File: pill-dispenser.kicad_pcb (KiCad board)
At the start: 2 copper layers, 50 x 50 mm, 34 parts, among them J1 USB-C, J2 Battery, J3 WS2812B, J4 Button, J5 Wakeup Button, Q1 AO3401A, Q2 FS8205A, U1 MT3608, U2 ESP32-C3-Zero, U3 TP4056-42-ESOP8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

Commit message: Working on 1.2 final version
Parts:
- removed J2: Battery, Connector_PinSocket_2.54mm:PinSocket_1x02_P2.54mm_Horizontal
- added BT1: Battery_Cell, Connector_PinHeader_2.54mm:PinHeader_1x02_P2.54mm_Vertical, F.Cu at (151.8, 119.7)
- added SW1: Battery Switch, EG1271:SW_EG1271, F.Cu at (150.5, 126.2)
- R11: value 1k -> 75K
- R8: value 300 -> 30K
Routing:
- net Net-(BT1--): track 0.00 -> 20.9 mm, vias 0 -> 2
- net Net-(U4-GND): track 20.5 -> 0.00 mm, vias 2 -> 0
- net VBAT: track 76.9 -> 70.6 mm, vias 2 -> 3
- net Net-(U4-VCC): track 14.6 -> 13.8 mm
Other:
- board text added: "I-Pat, LLC REV: 1.2"
- board text removed: "Telepat, LLC REV: 1.1"

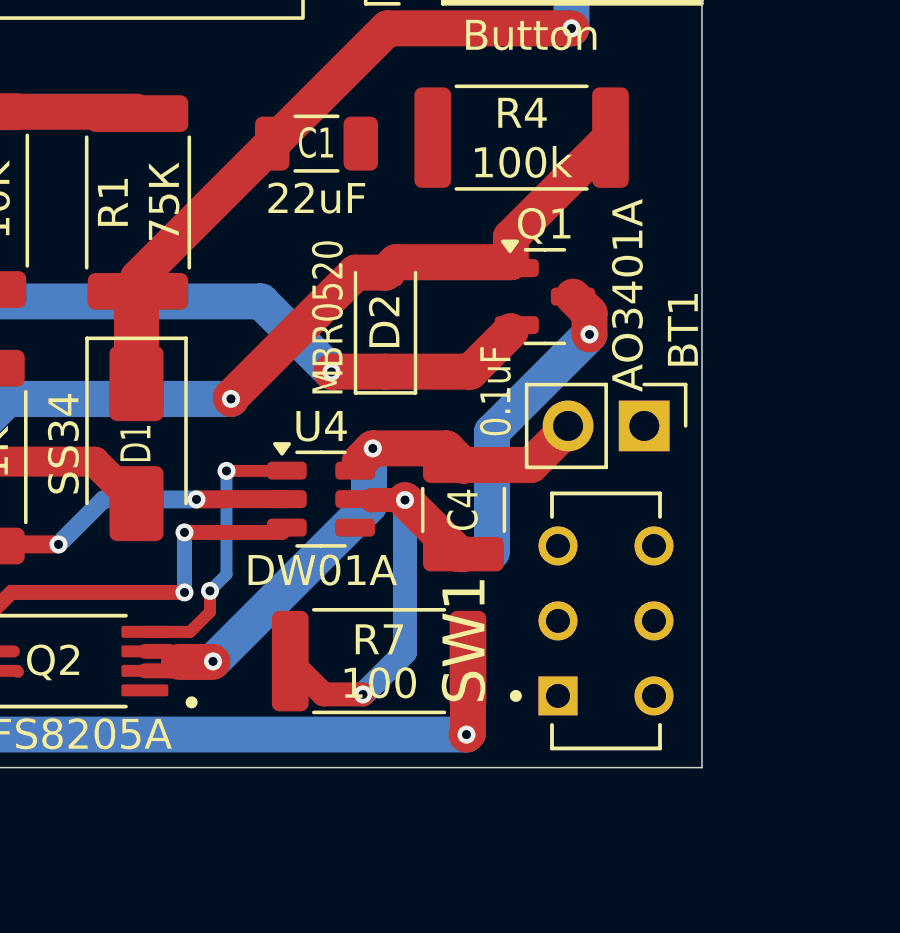
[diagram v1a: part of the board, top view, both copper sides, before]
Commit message: Updated pcb to rev1.2
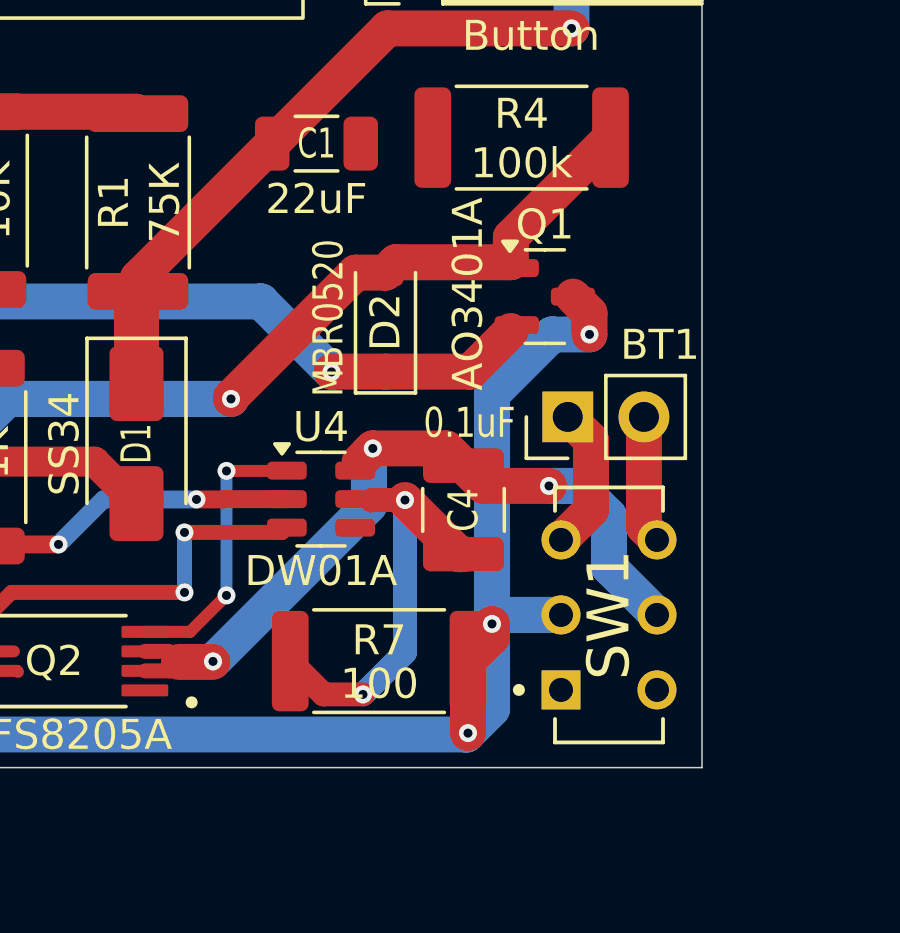
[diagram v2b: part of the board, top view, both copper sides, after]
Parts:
- moved BT1 2.57 mm to (149.2, 119.4), turned to 90 degrees
- moved SW1 0.22 mm to (150.6, 126.0)
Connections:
- SW1 pad 1: VBAT -> unconnected-(SW1-Pad1)
- SW1 pad 2: Net-(BT1-+) -> VBAT
- SW1 pad 3: unconnected-(SW1-Pad3) -> Net-(BT1-+)
- SW1 pad 4: Net-(U4-GND) -> unconnected-(SW1-Pad4)
- SW1 pad 5: Net-(BT1--) -> Net-(U4-GND)
- SW1 pad 6: unconnected-(SW1-Pad6) -> Net-(BT1--)
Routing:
- net Net-(U4-GND): track 0.00 -> 26.4 mm, vias 0 -> 3
- net Net-(BT1--): track 20.9 -> 4.28 mm, vias 2 -> 0
- net VBAT: track 70.6 -> 81.7 mm, vias 3 -> 4
- net Net-(BT1-+): track 0.00 -> 4.84 mm

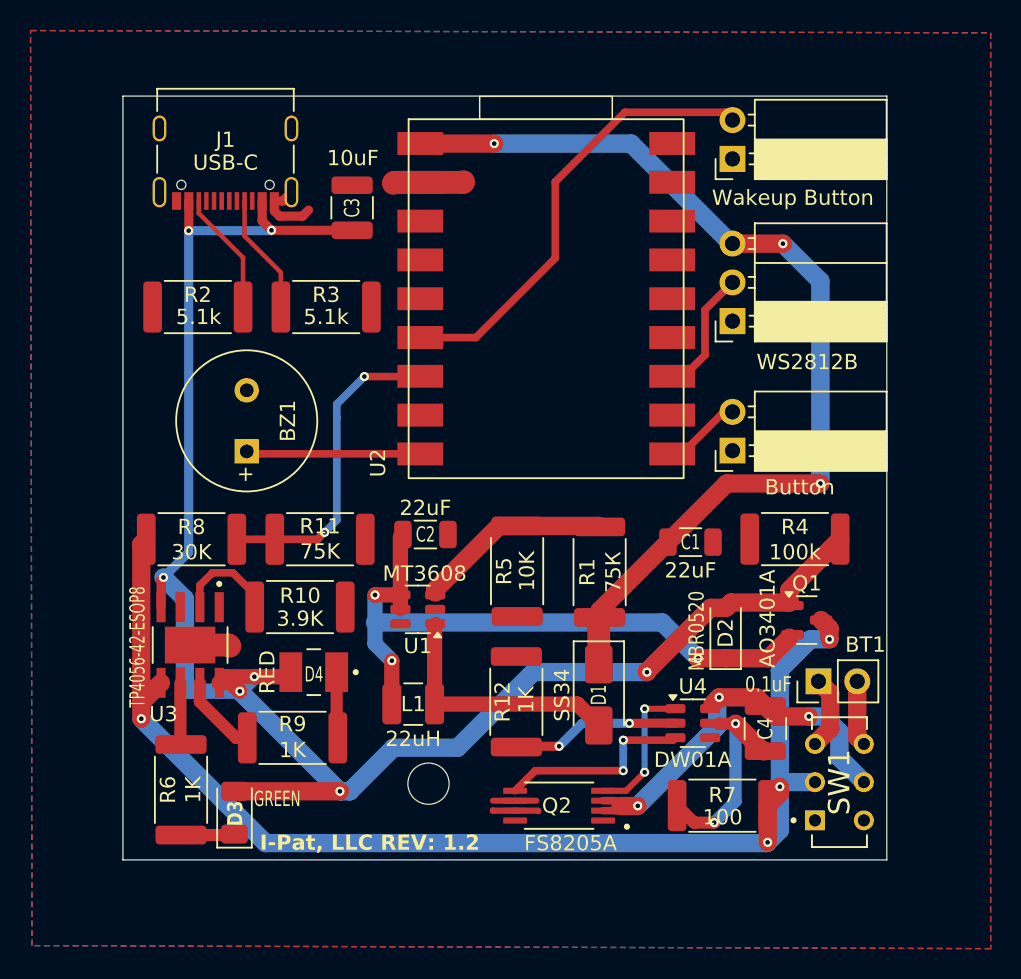
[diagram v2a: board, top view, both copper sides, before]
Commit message: Added control led strip transotor, placed buttons on PCB
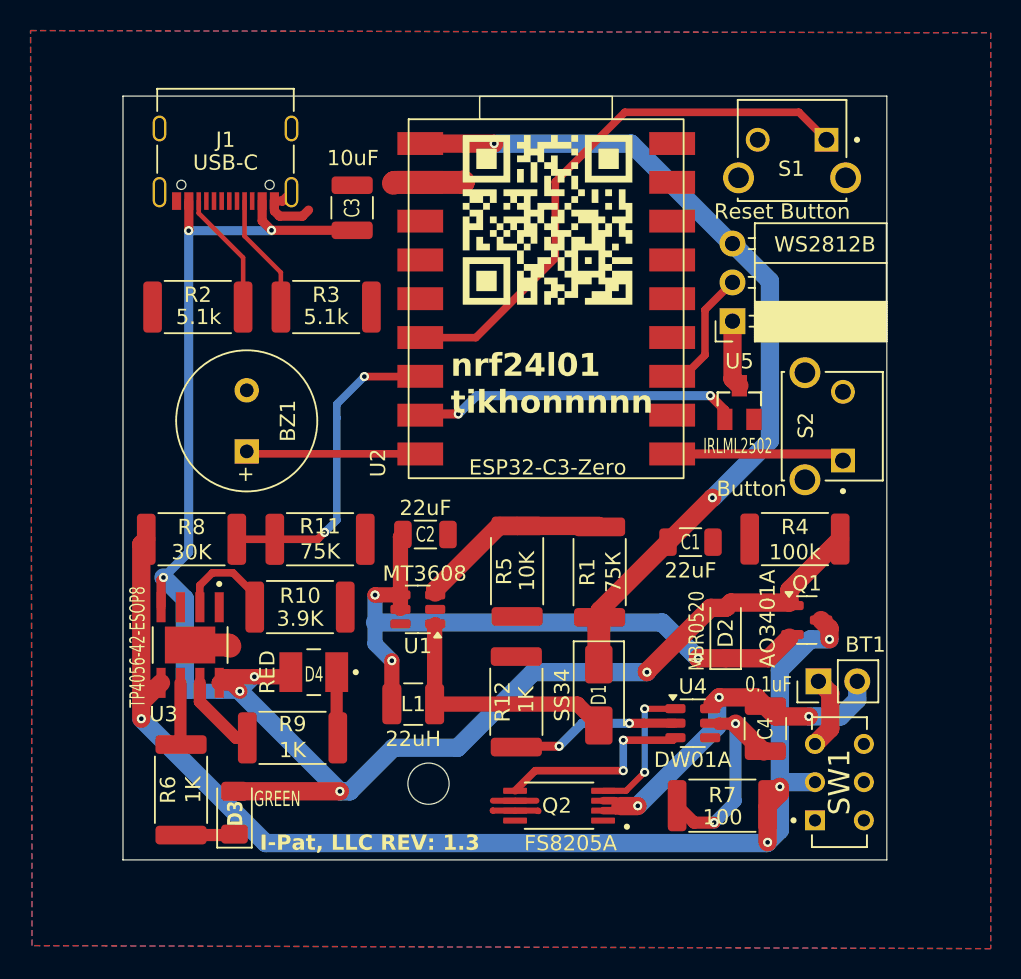
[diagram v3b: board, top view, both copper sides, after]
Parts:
- removed J4: Button, Connector_PinSocket_2.54mm:PinSocket_1x02_P2.54mm_Horizontal
- removed J5: Wakeup Button, Connector_PinSocket_2.54mm:PinSocket_1x02_P2.54mm_Horizontal
- added S1: Reset Button, FSMRA6JH:SW_FSMRA6JH, F.Cu at (147.5, 84.0)
- added S2: Button, FSMRA6JH:SW_FSMRA6JH, F.Cu at (150.8, 102.7)
- added U5: IRLML2502, IRLML2502TRPBF:SOT23, F.Cu at (144.1, 101.2)
- added qr: , LOGO, F.Cu at (131.5, 89.2)
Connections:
- net /LED_STRIP renamed /LED_STRIP_CONTROL
- C4 pad 2: Net-(U4-GND) -> Net-(BT1--)
- J3 pad 1: GND -> Net-(J3-Pin_1)
- Q2 pad 2: Net-(U4-GND) -> Net-(BT1--)
- Q2 pad 3: Net-(U4-GND) -> Net-(BT1--)
- SW1 pad 5: Net-(U4-GND) -> unconnected-(SW1-Pad5)
- SW1 pad 6: Net-(BT1--) -> unconnected-(SW1-Pad6)
- U2 pad 8: unconnected-(U2-IO4-Pad8) -> /LED_STRIP_ENABLE
- U4 pad 6: Net-(U4-GND) -> Net-(BT1--)
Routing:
- net Net-(U4-GND): track 26.4 -> 0.00 mm, vias 3 -> 0
- net /LED_STRIP_ENABLE: track 0.00 -> 21.5 mm, vias 0 -> 2
- net Net-(BT1--): track 4.28 -> 24.8 mm, vias 0 -> 3
- net +5V: track 64.5 -> 56.2 mm, vias 3 -> 2
- net /BUTTON: track 5.29 -> 12.2 mm
- net /WAKEUP_BUT: track 29.7 -> 36.4 mm
- net Net-(J3-Pin_1): track 0.00 -> 4.41 mm
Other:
- board text added: "I-Pat, LLC REV: 1.3"
- board text added: "nrf24l01 tikhonnnnn"
- board text removed: "I-Pat, LLC REV: 1.2"
